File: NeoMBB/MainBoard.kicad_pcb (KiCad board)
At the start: 4 copper layers, 120 x 105 mm, 105 parts, among them IC1 MCP2515-e_ST, IC2 ISO1042BDWVR, IC3 MCP2515-e_ST, IC4 ISO1042BDWVR, J2 TBP01R2-508-06BE, J3 TBP01R1-508-08BE, J4 TBP01R2-508-04BE, J5 TBP01R2-508-04BE, Q1 SIHFR120-GE3, Q2 SIHFR120-GE3, U1 TCMT1100, U11 TCMT1100, U12 BTS462TATMA1, U2 TCMT1100, U3 TCMT1100, U4 TCMT1100, U5 BTS462TATMA1, U6 TCMT1100, U7 TCMT1100, U9 TCMT1100, Y1 8MHz, Y2 8MHz

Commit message: Probed Zero wiring harness
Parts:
- removed C31, C32, C33, C34, C35, C36, C37, C38, C39, C40, C41, C42: UCM1H101MCL1GS, InverterCom:CAPAE660X800N
- removed D1, D2, D3, D4: SM6T15A, Diode_SMD:D_SMB
- removed J5: TBP01R2-508-04BE, InverterCom:SHDR4W100P0X508_1X4_2192X850X1200P
- removed Q2: SIHFR120-GE3, InverterCom:SIHFR120GE3
- removed R12, R16, R19, R24: 1k, Resistor_SMD:R_1210_3225Metric_Pad1.30x2.65mm_HandSolder
- removed R13, R14, R15, R17, R18, R20, R21, R25, R26: 4.7k, Resistor_SMD:R_1210_3225Metric_Pad1.30x2.65mm_HandSolder
- removed R22, R23: 120, Resistor_SMD:R_1210_3225Metric_Pad1.30x2.65mm_HandSolder
- removed U1, U11, U2, U3, U4, U6, U7, U9: TCMT1100, Package_SO:SOP-4_4.4x2.6mm_P1.27mm
- removed U12, U5: BTS462TATMA1, Package_TO_SOT_SMD:TO-252-4
- added C43: 100nF, Capacitor_SMD:C_1210_3225Metric_Pad1.33x2.70mm_HandSolder, F.Cu at (-38.6, 124.5)
- added C44: 22pF, Capacitor_SMD:C_1210_3225Metric_Pad1.33x2.70mm_HandSolder, F.Cu at (-38.6, 128.8)
- added C45: 10uF, Capacitor_SMD:C_1210_3225Metric_Pad1.33x2.70mm_HandSolder, F.Cu at (-38.6, 133.0)
- added C46: 10uF, Capacitor_SMD:C_1210_3225Metric_Pad1.33x2.70mm_HandSolder, F.Cu at (-38.6, 137.3)
- added C47: 10uF, Capacitor_SMD:C_1210_3225Metric_Pad1.33x2.70mm_HandSolder, F.Cu at (-38.6, 141.5)
- added C48: 22pF, Capacitor_SMD:C_1210_3225Metric_Pad1.33x2.70mm_HandSolder, F.Cu at (-32.6, 124.5)
- added C49: 100nF, Capacitor_SMD:C_1210_3225Metric_Pad1.33x2.70mm_HandSolder, F.Cu at (-32.6, 128.8)
- added C50: 100nF, Capacitor_SMD:C_1210_3225Metric_Pad1.33x2.70mm_HandSolder, F.Cu at (-32.6, 133.0)
- added C51: 10uF, Capacitor_SMD:C_1210_3225Metric_Pad1.33x2.70mm_HandSolder, F.Cu at (-32.6, 137.3)
- added C52: 100nF, Capacitor_SMD:C_1210_3225Metric_Pad1.33x2.70mm_HandSolder, F.Cu at (-32.6, 141.5)
- added C53: 22pF, Capacitor_SMD:C_1210_3225Metric_Pad1.33x2.70mm_HandSolder, F.Cu at (-26.6, 124.5)
- added C54: 22pF, Capacitor_SMD:C_1210_3225Metric_Pad1.33x2.70mm_HandSolder, F.Cu at (-26.6, 128.8)
- added C55: 22pF, Capacitor_SMD:C_1210_3225Metric_Pad1.33x2.70mm_HandSolder, F.Cu at (-26.6, 133.0)
- added C56: 100nF, Capacitor_SMD:C_1210_3225Metric_Pad1.33x2.70mm_HandSolder, F.Cu at (-38.6, 89.5)
- added C57: 22pF, Capacitor_SMD:C_1210_3225Metric_Pad1.33x2.70mm_HandSolder, F.Cu at (-38.6, 93.7)
- added C58: 10uF, Capacitor_SMD:C_1210_3225Metric_Pad1.33x2.70mm_HandSolder, F.Cu at (-38.6, 98.0)
- added C59: 10uF, Capacitor_SMD:C_1210_3225Metric_Pad1.33x2.70mm_HandSolder, F.Cu at (-38.6, 102.2)
- added C60: 10uF, Capacitor_SMD:C_1210_3225Metric_Pad1.33x2.70mm_HandSolder, F.Cu at (-38.6, 106.5)
- added C61: 22pF, Capacitor_SMD:C_1210_3225Metric_Pad1.33x2.70mm_HandSolder, F.Cu at (-32.6, 89.5)
- added C62: 100nF, Capacitor_SMD:C_1210_3225Metric_Pad1.33x2.70mm_HandSolder, F.Cu at (-32.6, 93.7)
- added C63: 100nF, Capacitor_SMD:C_1210_3225Metric_Pad1.33x2.70mm_HandSolder, F.Cu at (-32.6, 98.0)
- added C64: 10uF, Capacitor_SMD:C_1210_3225Metric_Pad1.33x2.70mm_HandSolder, F.Cu at (-32.6, 102.2)
- added C65: 100nF, Capacitor_SMD:C_1210_3225Metric_Pad1.33x2.70mm_HandSolder, F.Cu at (-32.6, 106.5)
- added C66: 22pF, Capacitor_SMD:C_1210_3225Metric_Pad1.33x2.70mm_HandSolder, F.Cu at (-26.6, 89.5)
- added C67: 22pF, Capacitor_SMD:C_1210_3225Metric_Pad1.33x2.70mm_HandSolder, F.Cu at (-26.6, 93.7)
- added C68: 22pF, Capacitor_SMD:C_1210_3225Metric_Pad1.33x2.70mm_HandSolder, F.Cu at (-26.6, 98.0)
- added C76: 10nF, Capacitor_SMD:C_1210_3225Metric_Pad1.33x2.70mm_HandSolder, F.Cu at (-55.3, 128.1)
- added C77: 10nF, Capacitor_SMD:C_1210_3225Metric_Pad1.33x2.70mm_HandSolder, F.Cu at (-55.3, 132.4)
- added C78: 10nF, Capacitor_SMD:C_1210_3225Metric_Pad1.33x2.70mm_HandSolder, F.Cu at (-55.3, 136.6)
- added C79: 10nF, Capacitor_SMD:C_1210_3225Metric_Pad1.33x2.70mm_HandSolder, F.Cu at (-55.3, 140.9)
- added FL3: ACT45B-101-2P-TL003, InverterCom:ACT45B1012PTL003, F.Cu at (-14.8, 113.8)
- added FL4: ACT45B-101-2P-TL003, InverterCom:ACT45B1012PTL003, F.Cu at (-14.8, 78.7)
- added IC10: DRDNB21D-7, InverterCom:SOT65P210X110-6N, B.Cu at (91.0, 22.5)
- added IC11: DRDNB21D-7, InverterCom:SOT65P210X110-6N, B.Cu at (113.5, 33.1)
- added IC5: MCP2515-e_ST, InverterCom:SOP65P640X120-20N, F.Cu at (-19.1, 140.2)
- added IC6: ISO1042BDWVR, InverterCom:SOIC127P1150X280-8N, F.Cu at (-16.7, 125.9)
- added IC7: MCP2515-e_ST, InverterCom:SOP65P640X120-20N, F.Cu at (-19.1, 105.2)
- added IC8: ISO1042BDWVR, InverterCom:SOIC127P1150X280-8N, F.Cu at (-16.7, 90.9)
- added IC9: MCP23S17-E_SO, InverterCom:SOIC127P1030X265-28N, F.Cu at (122.2, 58.1)
- added J1: MX23A34NF1, InverterCom:MX23A34NF1, F.Cu at (115.0, -6.00)
- added JP1: Jumper_2_Open, Jumper:SolderJumper-3_P2.0mm_Open_TrianglePad1.0x1.5mm, F.Cu at (22.5, 22.5)
- added JP2: Jumper_2_Open, Jumper:SolderJumper-3_P2.0mm_Open_TrianglePad1.0x1.5mm, F.Cu at (22.5, 26.4)
- added JP3: Jumper_2_Open, Jumper:SolderJumper-3_P2.0mm_Open_TrianglePad1.0x1.5mm, F.Cu at (22.5, 30.2)
- added JP4: Jumper_2_Open, Jumper:SolderJumper-3_P2.0mm_Open_TrianglePad1.0x1.5mm, F.Cu at (22.5, 34.1)
- added K1: AWHSH105D00G, InverterCom:AWHSH105D00G, F.Cu at (108.3, 16.5)
- added K2: AWHSH105D00G, InverterCom:AWHSH105D00G, F.Cu at (74.2, 28.5)
- added K3: AWHSH105D00G, InverterCom:AWHSH105D00G, F.Cu at (52.8, 28.5)
- added K4: AWHSH105D00G, InverterCom:AWHSH105D00G, F.Cu at (119.2, 28.5)
- added PS5: RKE-1205S_H, InverterCom:RKE1205SH, F.Cu at (-38.0, 115.0)
- added PS6: RKE-1205S_H, InverterCom:RKE1205SH, F.Cu at (-38.0, 80.0)
- added R27: 4.7k, Resistor_SMD:R_1210_3225Metric_Pad1.30x2.65mm_HandSolder, F.Cu at (-11.7, 138.2)
- added R28: 120, Resistor_SMD:R_1210_3225Metric_Pad1.30x2.65mm_HandSolder, F.Cu at (-11.7, 142.5)
- added R29: 4.7k, Resistor_SMD:R_1210_3225Metric_Pad1.30x2.65mm_HandSolder, F.Cu at (-11.7, 103.2)
- added R30: 120, Resistor_SMD:R_1210_3225Metric_Pad1.30x2.65mm_HandSolder, F.Cu at (-11.7, 107.4)
- added R38: 10k, Resistor_SMD:R_1210_3225Metric_Pad1.30x2.65mm_HandSolder, F.Cu at (-82.8, 88.7)
- added R40: 1k, Resistor_SMD:R_1210_3225Metric_Pad1.30x2.65mm_HandSolder, F.Cu at (-49.4, 128.1)
- added R41: 1k, Resistor_SMD:R_1210_3225Metric_Pad1.30x2.65mm_HandSolder, F.Cu at (-49.4, 132.3)
- added R42: 1k, Resistor_SMD:R_1210_3225Metric_Pad1.30x2.65mm_HandSolder, F.Cu at (-49.4, 136.5)
- added R43: 1k, Resistor_SMD:R_1210_3225Metric_Pad1.30x2.65mm_HandSolder, F.Cu at (-49.4, 140.7)
- added Y3: 8MHz, Crystal:Crystal_HC49-4H_Vertical, F.Cu at (-19.4, 132.8)
- added Y4: 8MHz, Crystal:Crystal_HC49-4H_Vertical, F.Cu at (-19.4, 97.8)
- added Z10: MMSZ5231B-TP, InverterCom:SOD3716X135N, F.Cu at (-61.4, 141.2)
- added Z11: MMSZ5231B-TP, InverterCom:SOD3716X135N, F.Cu at (-61.4, 121.8)
- added Z2: MMSZ5231B-TP, InverterCom:SOD3716X135N, F.Cu at (-61.4, 128.2)
- added Z5: MMSZ5231B-TP, InverterCom:SOD3716X135N, F.Cu at (-61.4, 108.7)
- added Z6: MMSZ5231B-TP, InverterCom:SOD3716X135N, F.Cu at (-61.4, 113.1)
- added Z7: MMSZ5231B-TP, InverterCom:SOD3716X135N, F.Cu at (-61.4, 117.4)
- added Z8: MMSZ5231B-TP, InverterCom:SOD3716X135N, F.Cu at (-61.4, 132.5)
- added Z9: MMSZ5231B-TP, InverterCom:SOD3716X135N, F.Cu at (-61.4, 136.9)
- A1: footprint Module:RaspberryPi_Pico_Common_Unspecified -> Module:RaspberryPi_Pico_Common_THT
- C1, C10, C11, C12, C15, C16, C17, C19, C2, C20, C21, C22, C23, C24, C25, C3, C4, C5, C6, C7, C8, C9, R2, R3, R4: moved to F.Cu
- C27, C28, C29, C30: value UCM1H101MCL1GS -> 10nF; footprint InverterCom:CAPAE660X800N -> Capacitor_SMD:C_1210_3225Metric_Pad1.33x2.70mm_HandSolder
- J2: value TBP01R2-508-06BE -> MX23A40NF1; footprint InverterCom:TBP01R250806BE -> InverterCom:MX23A40NF1
- J3: value TBP01R1-508-08BE -> TBP02R2W-381-06BE; footprint InverterCom:SHDR8W100P0X508_1X8_4224X1200X890P -> InverterCom:TBP02R2W38106BE
- PS1: value SCW20A-12 -> OKI-78SR-5_1.5-W36E-C; footprint InverterCom:SCW20A12 -> InverterCom:OKI78SR515W36EC
- PS4: value R-78K3.3-1.0 -> EC7BW-110S12; footprint InverterCom:R78K3310 -> InverterCom:EC7BW110S12; moved to B.Cu
- Q1: value SIHFR120-GE3 -> TBD62783AFG,EL; footprint InverterCom:SIHFR120GE3 -> InverterCom:SOIC127P1030X245-18N; moved to B.Cu
- R10: value 4.7k -> 0
- R11, R9: value 1k -> 0
- R6, R8: value 4.7k -> 1k
- moved C24 198.3 mm to (-84.4, 119.5)
- moved C25 197.4 mm to (-84.4, 123.7), turned to 0 degrees
- moved C26 193.9 mm to (-84.4, 128.0), turned to 0 degrees
- moved C23 192.2 mm to (-90.4, 136.5), turned to 0 degrees
- moved C22 186.9 mm to (-90.4, 132.2), turned to 0 degrees
- moved C17 179.7 mm to (-96.4, 132.2)
- moved C16 179.0 mm to (-96.4, 128.0), turned to 0 degrees
- moved R4 177.5 mm to (-69.5, 137.4), turned to 0 degrees
- moved C21 176.7 mm to (-90.4, 128.0), turned to 0 degrees
- moved C15 175.0 mm to (-96.4, 123.7), turned to 0 degrees
- moved R9 174.6 mm to (-82.8, 76.0), turned to 0 degrees
- moved R11 173.6 mm to (-82.8, 84.5), turned to 0 degrees
- moved PS3 171.9 mm to (-95.9, 110.0)
- moved C18 171.3 mm to (-96.4, 136.5), turned to 0 degrees
- moved H2 170.7 mm to (152.5, 7.50)
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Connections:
- A1 pad 10: /CHARGER_OUT_SS1 -> /CAN2_INT
- A1 pad 11: /CHARGER_OUT_SS2 -> /UART_TX
- A1 pad 12: /CHARGER_IN_DCP -> /UART_RX
- A1 pad 13: /GND_A -> /12V_GND
- A1 pad 14: /CAN2_SPI_SCK -> /MCP_SPI_SCK
- A1 pad 15: /CAN2_SPI_TX -> /MCP_SPI_TX
- A1 pad 16: /CAN2_SPI_RX -> /MCP_SPI_RX
- A1 pad 17: /CAN2_INT -> /CAN2_CS
- A1 pad 18: /GND_A -> /12V_GND
- A1 pad 19: /CAN2_CS -> /CAN3_INT
- A1 pad 20: /CONTACTOR_OUT -> /CAN3_CS
- A1 pad 21: /VEHICLE_IN_SS1 -> /CAN4_CS
- A1 pad 22: /VEHICLE_IN_SS2 -> /CAN4_INT
- A1 pad 23: /GND_A -> /12V_GND
- A1 pad 24: /VEHICLE_IN_PP -> /MCP_SPI_CS
- A1 pad 25: /VEHICLE_OUT_DCP -> /MCP_SPI_INTA
- A1 pad 26: unconnected-(A1-GPIO20-Pad26) -> /MCP_SPI_INTB
- A1 pad 27: unconnected-(A1-GPIO21-Pad27) -> /MCP_SPI_RST
- A1 pad 28: /GND_A -> /12V_GND
- A1 pad 29: unconnected-(A1-GPIO22-Pad29) -> /MTR_CTRL_ENABLE_SIGNAL
- A1 pad 3: /GND_A -> /12V_GND
- A1 pad 31: unconnected-(A1-GPIO26_ADC0-Pad31) -> /AMBIENT_TEMP
- A1 pad 33: /GND_A -> /12V_GND
- A1 pad 38: /GND_A -> /12V_GND
- A1 pad 4: /CAN1_SPI_SCK -> /CAN_SPI_SCK
- A1 pad 5: /CAN1_SPI_TX -> /CAN_SPI_TX
- A1 pad 6: /CAN1_SPI_RX -> /CAN_SPI_RX
- A1 pad 8: /GND_A -> /12V_GND
- C1 pad 2: /GND_A -> /12V_GND
- C10 pad 1: /Isolated Canbus Module/CAN_GND -> /CAN0_GND
- C10 pad 2: /Isolated Canbus Module/CAN_5V -> /CAN0_+5V
- C11 pad 1: /Isolated Canbus Module/CAN_GND -> /CAN0_GND
- C11 pad 2: /Isolated Canbus Module/CAN_H_B -> /CAN0_HIGH
- C12 pad 1: /Isolated Canbus Module/CAN_L_B -> /CAN0_LOW
- C12 pad 2: /Isolated Canbus Module/CAN_GND -> /CAN0_GND
- C13 pad 1: /Isolated Canbus Module/CAN_H_B -> /CAN0_HIGH
- C13 pad 2: /Isolated Canbus Module/CAN_L_B -> /CAN0_LOW
- C14 pad 2: /GND_A -> /12V_GND
- C15 pad 2: /GND_A -> /12V_GND
- C16 pad 1: /GND_A -> /12V_GND
- C17 pad 2: /GND_A -> /12V_GND
- C18 pad 2: /GND_A -> /12V_GND
- C19 pad 2: /GND_A -> /12V_GND
- C2 pad 2: /GND_A -> /12V_GND
- C20 pad 2: /GND_A -> /12V_GND
- C21 pad 2: /GND_A -> /12V_GND
- C22 pad 2: /CHAdeMO_FG -> /CAN1_GND
- C23 pad 1: /CHAdeMO_FG -> /CAN1_GND
- C24 pad 1: /CHAdeMO_FG -> /CAN1_GND
- C24 pad 2: /CHAdeMO_CAN_H -> /CAN1_HIGH
- C25 pad 1: /CHAdeMO_CAN_L -> /CAN1_LOW
- C25 pad 2: /CHAdeMO_FG -> /CAN1_GND
- C26 pad 1: /CHAdeMO_CAN_H -> /CAN1_HIGH
- C26 pad 2: /CHAdeMO_CAN_L -> /CAN1_LOW
- C27 pad 1: /+12V_A -> /KICKSTAND_SW_FILTERED
- C27 pad 2: /GND_A -> /12V_GND
- C28 pad 1: /+12V_A -> /HVIL_SIG_FILTERED
- C28 pad 2: /GND_A -> /12V_GND
- C29 pad 1: /+12V_A -> /MTR_STOP_SW_SIGNAL
- C29 pad 2: /GND_A -> /12V_GND
- C3 pad 1: /GND_A -> /12V_GND
- C30 pad 1: /+12V_A -> /START_SW_INPUT_SIGNAL
- C30 pad 2: /GND_A -> /12V_GND
- C4 pad 2: /GND_A -> /12V_GND
- C5 pad 2: /GND_A -> /12V_GND
- C6 pad 2: /GND_A -> /12V_GND
- C7 pad 2: /GND_A -> /12V_GND
- C8 pad 2: /GND_A -> /12V_GND
- C9 pad 1: /Isolated Canbus Module/CAN_5V -> /CAN0_+5V
- C9 pad 2: /Isolated Canbus Module/CAN_GND -> /CAN0_GND
- FL1 pad 3: /Isolated Canbus Module/CAN_L_B -> /CAN0_LOW
- FL1 pad 4: /Isolated Canbus Module/CAN_H_B -> /CAN0_HIGH
- FL2 pad 3: /CHAdeMO_CAN_L -> /CAN1_LOW
- FL2 pad 4: /CHAdeMO_CAN_H -> /CAN1_HIGH
- IC1 pad 10: /GND_A -> /12V_GND
- IC1 pad 14: /CAN1_SPI_SCK -> /CAN_SPI_SCK
- IC1 pad 16: /CAN1_SPI_TX -> /CAN_SPI_TX
- IC1 pad 17: /CAN1_SPI_RX -> /CAN_SPI_RX
- IC2 pad 4: /GND_A -> /12V_GND
- IC2 pad 5: /Isolated Canbus Module/CAN_GND -> /CAN0_GND
- IC2 pad 8: /Isolated Canbus Module/CAN_5V -> /CAN0_+5V
- IC3 pad 10: /GND_A -> /12V_GND
- IC3 pad 14: /CAN2_SPI_SCK -> /CAN_SPI_SCK
- IC3 pad 16: /CAN2_SPI_TX -> /CAN_SPI_TX
- IC3 pad 17: /CAN2_SPI_RX -> /CAN_SPI_RX
- IC4 pad 4: /GND_A -> /12V_GND
- IC4 pad 5: /CHAdeMO_FG -> /CAN1_GND
- J2 pad 1: /Isolated Canbus Module/CAN_5V -> /MOTOR_CONTR_GND
- J2 pad 2: /Isolated Canbus Module/CAN_GND -> /MOTOR_CONTR_+24V_IN
- J2 pad 3: /Isolated Canbus Module/CAN_H_B -> /CAN0_GND
- J2 pad 4: /Isolated Canbus Module/CAN_JUMPER_B -> /CAN0_+5V
- J2 pad 5: /Isolated Canbus Module/CAN_L_B -> /CAN1_GND
- J2 pad 6: /Isolated Canbus Module/CAN_H_B -> /CAN2_HIGH
- J3 pad 1: /CHAdeMO_FG -> unconnected-(J3-Pad1)
- J3 pad 2: /CHAdeMO_SS1 -> unconnected-(J3-Pad2)
- J3 pad 3: /CHAdeMO_SS2 -> /CAN2_GND
- J3 pad 4: /CHAdeMO_NC -> /CAN2_+5V
- J3 pad 5: /CHAdeMO_DCP -> /CAN2_HIGH
- J3 pad 6: /CHAdeMO_PP -> /CAN2_LOW
- J4 pad 1: /GND_A -> /12V_GND
- J4 pad 3: /GND_A -> /12V_GND
- PS1 pad 1: unconnected-(PS1-REMOTE_ON/OFF-Pad1) -> /+12V_A
- PS1 pad 2: /GND_A -> /12V_GND
- PS1 pad 3: /GND_A -> /+5V_A
- PS2 pad 2: /GND_A -> /12V_GND
- PS2 pad 5: /Isolated Canbus Module/CAN_GND -> /CAN0_GND
- PS2 pad 7: /Isolated Canbus Module/CAN_5V -> /CAN0_+5V
- PS3 pad 2: /GND_A -> /12V_GND
- PS3 pad 5: /CHAdeMO_FG -> /CAN1_GND
- PS4 pad 1: /+12V_A -> /MBB_LOW_PWR
- PS4 pad 2: /GND_A -> /POWER_PACK_GND
- PS4 pad 3: /+3.3V_A -> /+12V_A
- Q1 pad 1: Net-(Q1-G) -> /SIG_ABS_LIGHT
- Q1 pad 2: /CHAdeMO_FG -> /SIG_CHARGING_RED
- Q1 pad 3: /CHAdeMO_SS2 -> /SIG_CHARGING
- R10 pad 1: /+3.3V_A -> /POWER_PACK_GND
- R10 pad 2: /CHARGER_IN_DCP -> /HighSideOutputs/RELAY_3_COM
- R11 pad 1: /+12V_CHAdeMO -> /KEY_ON_12V
- R11 pad 2: Net-(R11-Pad2) -> /+12V_A
- R2 pad 2: /Isolated Canbus Module/CAN_L_B -> /CAN0_LOW
- R4 pad 1: /CHAdeMO_CAN_H -> /Isolated Canbus Module1/CAN_JUMPER_B
- R4 pad 2: /CHAdeMO_CAN_L -> /CAN1_LOW
- R5 pad 1: /CHAdeMO_SS1 -> /KICKSTAND_SW_FILTERED
- R5 pad 2: Net-(R5-Pad2) -> /KICKSTAND_SW_SIG
- R6 pad 1: /+3.3V_A -> /HVIL_SIG_FILTERED
- R6 pad 2: /VEHICLE_IN_SS1 -> /HVIL_RETURN
- R7 pad 1: /CHAdeMO_SS1 -> /MTR_STOP_SW_SIGNAL
- R7 pad 2: Net-(R7-Pad2) -> /MTR_STOP_SW_IN
- R8 pad 1: /+3.3V_A -> /START_SW_INPUT_SIGNAL
- R8 pad 2: /VEHICLE_IN_SS2 -> /START_SW_INPUT
- R9 pad 1: /+12V_CHAdeMO -> /MBB_LOW_PWR
- R9 pad 2: Net-(R9-Pad2) -> /HighSideOutputs/RELAY_3_COM
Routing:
- net /+12V_A: track 99.2 -> 0.00 mm, vias 10 -> 0
- net /CHARGER_OUT_SS1: track 85.4 -> 0.00 mm
- net /CHARGER_OUT_SS2: track 78.4 -> 0.00 mm, vias 1 -> 0
- net /CAN1_CS: track 77.7 -> 0.00 mm, vias 3 -> 0
- net /CAN1_INT: track 72.9 -> 0.00 mm
- net /CAN1_SPI_RX: track 71.8 -> 0.00 mm, vias 1 -> 0
- net /CHARGER_IN_DCP: track 70.1 -> 0.00 mm, vias 3 -> 0
- net /CAN1_SPI_TX: track 65.6 -> 0.00 mm, vias 2 -> 0
- net /CAN1_SPI_SCK: track 64.2 -> 0.00 mm
- net /VEHICLE_IN_PP: track 58.0 -> 0.00 mm, vias 6 -> 0
- net /CHAdeMO_SS1: track 57.8 -> 0.00 mm, vias 4 -> 0
- net /+3.3V_A: track 55.6 -> 0.00 mm, vias 13 -> 0
- net /CHAdeMO_SS2: track 51.4 -> 0.00 mm, vias 5 -> 0
- net /VEHICLE_IN_SS2: track 50.6 -> 0.00 mm, vias 6 -> 0
- net /Isolated Canbus Module/CAN_H_B: track 46.5 -> 0.00 mm, vias 1 -> 0
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- removed copper zone on In2.Cu, net /+12V_A
- removed copper zone on In2.Cu, net /+12V_CHAdeMO
- removed copper zone on In2.Cu, net /+3.3V_A
- removed copper zone on B.Cu, net /CHAdeMO_FG
- removed copper zone on F.Cu, net /CHAdeMO_FG
- removed copper zone on In1.Cu, net /CHAdeMO_FG
- removed copper zone on B.Cu, net /GND_A
- removed copper zone on F.Cu, net /GND_A
- removed copper zone on In1.Cu, net /GND_A
- removed copper zone on B.Cu, net /Isolated Canbus Module/CAN_GND
- removed copper zone on F.Cu, net /Isolated Canbus Module/CAN_GND
- removed copper zone on In1.Cu, net /Isolated Canbus Module/CAN_GND
- removed copper zone on In2.Cu, net /Isolated Canbus Module/CAN_GND
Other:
- board size 120 x 105 mm -> 160 x 80 mm
- copper layers 4 -> 6
- board text removed: "->"
- board text removed: "CHAdeMO INTERFACE BOARD CAN FUNCTION AS STATION OR VEHICLE"
- board text removed: "CHAdeMO PP RESISTOR (CHARGER SIDE ONLY)"
- board text removed: "| +5V | GND | JP1 | JP2 | CANL | CANH | CAN 1 INTERFACE"
- board text removed: "| A | B | A | B | 12V <1.5A CONTACTOR COIL"
- board text removed: "| FG | SS1 | SS2 | NC | DCP | PP | CANH| CANL| CHAdeMO SIGNAL PINS"
- board text removed: "| GND | +12V | GND | +12V | 12V INPUT"

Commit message: MBB Reverse engineering bs
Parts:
- removed C27, C28, C29, C30, C76, C77, C78, C79: 10nF, Capacitor_SMD:C_1210_3225Metric_Pad1.33x2.70mm_HandSolder
- removed C58, C59, C60, C64: 10uF, Capacitor_SMD:C_1210_3225Metric_Pad1.33x2.70mm_HandSolder
- removed C61, C66, C67, C68: 22pF, Capacitor_SMD:C_1210_3225Metric_Pad1.33x2.70mm_HandSolder
- removed C62, C63, C65: 100nF, Capacitor_SMD:C_1210_3225Metric_Pad1.33x2.70mm_HandSolder
- removed J3: TBP02R2W-381-06BE, InverterCom:TBP02R2W38106BE
- removed K3, K4: AWHSH105D00G, InverterCom:AWHSH105D00G
- removed R41, R42, R43: 1k, Resistor_SMD:R_1210_3225Metric_Pad1.30x2.65mm_HandSolder
- removed Z10, Z11, Z2, Z5, Z6, Z7, Z8, Z9: MMSZ5231B-TP, InverterCom:SOD3716X135N
- added C31: 100nF, Capacitor_SMD:C_1210_3225Metric_Pad1.33x2.70mm_HandSolder, B.Cu at (17.0, 79.6)
- added C32: 22pF, Capacitor_SMD:C_1210_3225Metric_Pad1.33x2.70mm_HandSolder, B.Cu at (17.0, 63.6)
- added C33: 10uF, Capacitor_SMD:C_1210_3225Metric_Pad1.33x2.70mm_HandSolder, B.Cu at (21.0, 79.4)
- added C34: 10uF, Capacitor_SMD:C_1210_3225Metric_Pad1.33x2.70mm_HandSolder, B.Cu at (33.6, 68.0)
- added C35: 10uF, Capacitor_SMD:C_1210_3225Metric_Pad1.33x2.70mm_HandSolder, B.Cu at (33.0, 75.0)
- added C36: 22pF, Capacitor_SMD:C_1210_3225Metric_Pad1.33x2.70mm_HandSolder, B.Cu at (23.0, 63.4)
- added C37: 100nF, Capacitor_SMD:C_1210_3225Metric_Pad1.33x2.70mm_HandSolder, B.Cu at (28.0, 68.0)
- added C38: 100nF, Capacitor_SMD:C_1210_3225Metric_Pad1.33x2.70mm_HandSolder, B.Cu at (29.0, 75.0)
- added C39: 10uF, Capacitor_SMD:C_1210_3225Metric_Pad1.33x2.70mm_HandSolder, B.Cu at (45.0, 75.0)
- added C40: 100nF, Capacitor_SMD:C_1210_3225Metric_Pad1.33x2.70mm_HandSolder, B.Cu at (40.0, 74.6)
- added C41: 22pF, Capacitor_SMD:C_1210_3225Metric_Pad1.33x2.70mm_HandSolder, F.Cu at (53.0, 75.0)
- added C42: 22pF, Capacitor_SMD:C_1210_3225Metric_Pad1.33x2.70mm_HandSolder, B.Cu at (50.6, 77.0)
- added IC12: DRDNB21D-7, InverterCom:SOT65P210X110-6N, B.Cu at (76.0, 41.6)
- added IC13: DRDNB21D-7, InverterCom:SOT65P210X110-6N, B.Cu at (108.0, 23.0)
- added IC14: DRDNB21D-7, InverterCom:SOT65P210X110-6N, B.Cu at (109.0, 41.0)
- added IC15: MCP23S17-E_SO, InverterCom:SOIC127P1030X265-28N, F.Cu at (86.0, 62.0)
- added K5: AWHSH105D00G, InverterCom:AWHSH105D00G, F.Cu at (116.2, 47.0)
- added K6: AWHSH105D00G, InverterCom:AWHSH105D00G, F.Cu at (95.2, 29.0)
- added K7: AWHSH105D00G, InverterCom:AWHSH105D00G, F.Cu at (116.2, 29.0)
- added K8: AWHSH105D00G, InverterCom:AWHSH105D00G, F.Cu at (95.2, 47.0)
- added PS7: RD7-12S033R, InverterCom:RD712S033R, F.Cu at (156.6, 73.4)
- added PS8: RKE-1205S_H, InverterCom:RKE1205SH, F.Cu at (16.2, 92.1)
- added PS9: RKE-1205S_H, InverterCom:RKE1205SH, F.Cu at (38.0, 92.0)
- added R12: 4.7k, Resistor_SMD:R_1210_3225Metric_Pad1.30x2.65mm_HandSolder, F.Cu at (14.4, 79.0)
- added R13: 120, Resistor_SMD:R_1210_3225Metric_Pad1.30x2.65mm_HandSolder, B.Cu at (51.0, 67.0)
- added R14: 4.7k, Resistor_SMD:R_1210_3225Metric_Pad1.30x2.65mm_HandSolder, F.Cu at (41.0, 54.0)
- added R15: 120, Resistor_SMD:R_1210_3225Metric_Pad1.30x2.65mm_HandSolder, B.Cu at (41.0, 17.4)
- added R16: 0, Resistor_SMD:R_1210_3225Metric_Pad1.30x2.65mm_HandSolder, F.Cu at (-111.3, 134.2)
- added R17: 1k, Resistor_SMD:R_1210_3225Metric_Pad1.30x2.65mm_HandSolder, F.Cu at (-139.0, 140.8)
- added R18: 4.7k, Resistor_SMD:R_1210_3225Metric_Pad1.30x2.65mm_HandSolder, F.Cu at (-139.0, 145.0)
- added R19: 1k, Resistor_SMD:R_1210_3225Metric_Pad1.30x2.65mm_HandSolder, F.Cu at (-87.1, 120.3)
- added R20: 1k, Resistor_SMD:R_1210_3225Metric_Pad1.30x2.65mm_HandSolder, F.Cu at (-87.1, 124.5)
- added R21: 1k, Resistor_SMD:R_1210_3225Metric_Pad1.30x2.65mm_HandSolder, F.Cu at (-87.1, 128.7)
- added R22: 1k, Resistor_SMD:R_1210_3225Metric_Pad1.30x2.65mm_HandSolder, F.Cu at (-87.1, 132.9)
- added R23: 1k, Resistor_SMD:R_1210_3225Metric_Pad1.30x2.65mm_HandSolder, F.Cu at (-87.1, 137.1)
- added R24: 1k, Resistor_SMD:R_1210_3225Metric_Pad1.30x2.65mm_HandSolder, F.Cu at (-87.1, 141.4)
- added R25: 0, Resistor_SMD:R_1210_3225Metric_Pad1.30x2.65mm_HandSolder, F.Cu at (-14.6, -5.00)
- added R26: 0, Resistor_SMD:R_1210_3225Metric_Pad1.30x2.65mm_HandSolder, F.Cu at (-66.4, 2.69)
- added R31: 120, Resistor_SMD:R_1210_3225Metric_Pad1.30x2.65mm_HandSolder, F.Cu at (-52.5, -1.51)
- added R32: 120, Resistor_SMD:R_1210_3225Metric_Pad1.30x2.65mm_HandSolder, F.Cu at (-52.5, 2.69)
- added R33: 120, Resistor_SMD:R_1210_3225Metric_Pad1.30x2.65mm_HandSolder, F.Cu at (-52.5, 6.91)
- added R34: 1k, Resistor_SMD:R_1210_3225Metric_Pad1.30x2.65mm_HandSolder, F.Cu at (-52.5, 11.1)
- added R35: 1k, Resistor_SMD:R_1210_3225Metric_Pad1.30x2.65mm_HandSolder, F.Cu at (-52.5, 15.3)
- added R36: 1k, Resistor_SMD:R_1210_3225Metric_Pad1.30x2.65mm_HandSolder, F.Cu at (-52.5, 19.5)
- added R37: 1k, Resistor_SMD:R_1210_3225Metric_Pad1.30x2.65mm_HandSolder, F.Cu at (-46.5, -1.51)
- added R39: 1k, Resistor_SMD:R_1210_3225Metric_Pad1.30x2.65mm_HandSolder, F.Cu at (-46.5, 2.69)
- added R44: 1k, Resistor_SMD:R_1210_3225Metric_Pad1.30x2.65mm_HandSolder, F.Cu at (-46.5, 6.91)
- added R45: 4.7k, Resistor_SMD:R_1210_3225Metric_Pad1.30x2.65mm_HandSolder, F.Cu at (-46.5, 11.1)
- added R46: 4.7k, Resistor_SMD:R_1210_3225Metric_Pad1.30x2.65mm_HandSolder, F.Cu at (-46.5, 15.3)
- added R47: 10k, Resistor_SMD:R_1210_3225Metric_Pad1.30x2.65mm_HandSolder, F.Cu at (-46.5, 19.5)
- added R48: 1k, Resistor_SMD:R_1210_3225Metric_Pad1.30x2.65mm_HandSolder, F.Cu at (-40.6, -1.51)
- added R49: 1k, Resistor_SMD:R_1210_3225Metric_Pad1.30x2.65mm_HandSolder, F.Cu at (-40.6, 2.69)
- added R50: 1k, Resistor_SMD:R_1210_3225Metric_Pad1.30x2.65mm_HandSolder, F.Cu at (-40.6, 6.91)
- added R51: 1k, Resistor_SMD:R_1210_3225Metric_Pad1.30x2.65mm_HandSolder, F.Cu at (-40.6, 11.1)
- added R52: 4.7k, Resistor_SMD:R_1210_3225Metric_Pad1.30x2.65mm_HandSolder, F.Cu at (-40.6, 15.3)
- added R53: 0, Resistor_SMD:R_1210_3225Metric_Pad1.30x2.65mm_HandSolder, F.Cu at (-103.4, 130.0)
- added U1: TCMT1100, Package_SO:SOP-4_4.4x2.6mm_P1.27mm, F.Cu at (-146.7, 140.8)
- added U2: TCMT1100, Package_SO:SOP-4_4.4x2.6mm_P1.27mm, F.Cu at (-52.0, 37.0)
- added U3: TCMT1100, Package_SO:SOP-4_4.4x2.6mm_P1.27mm, F.Cu at (-39.8, 87.4)
- added U4: TCMT1100, Package_SO:SOP-4_4.4x2.6mm_P1.27mm, F.Cu at (-39.8, 91.5)
- added U5: TCMT1100, Package_SO:SOP-4_4.4x2.6mm_P1.27mm, F.Cu at (-39.8, 95.7)
- added Z1: MMSZ5231B-TP, InverterCom:SOD3716X135N, F.Cu at (-81.0, 137.0)
- added Z12: MMSZ5231B-TP, InverterCom:SOD3716X135N, F.Cu at (-34.5, 13.8)
- added Z13: MMSZ5231B-TP, InverterCom:SOD3716X135N, F.Cu at (-34.5, 18.1)
- added Z14: MMSZ5231B-TP, InverterCom:SOD3716X135N, F.Cu at (-34.5, 22.5)
- added Z15: MMSZ5231B-TP, InverterCom:SOD3716X135N, F.Cu at (-34.5, 26.8)
- added Z16: MMSZ5231B-TP, InverterCom:SOD3716X135N, F.Cu at (-34.5, 31.2)
- added Z3: MMSZ5231B-TP, InverterCom:SOD3716X135N, F.Cu at (-81.0, 141.3)
- added Z4: MMSZ5231B-TP, InverterCom:SOD3716X135N, F.Cu at (-34.5, 9.39)
- C1, C10, C11, C12, C14, C15, C16, C17, C18, C19, C2, C20, C21, C22, C23, C24, C25, C3, C4, C46, C47, C5, C50, C54, C55, C6, C7, C8, C9, R2, R4: moved to B.Cu
- C43, C49: value 100nF -> 22pF; moved to B.Cu
- C44, C53: value 22pF -> 100nF; moved to B.Cu
- C45: value 10uF -> 22pF; moved to B.Cu
- C48: value 22pF -> 10uF; moved to B.Cu
- C51: value 10uF -> 100nF; moved to B.Cu
- C52: value 100nF -> 10uF; moved to B.Cu
- C56: value 100nF -> 22pF
- C57: value 22pF -> 100nF
- IC10, PS4, Q1: moved to F.Cu
- R10, R9: value 0 -> 1k
- R27, R29: value 4.7k -> 1k
- R28: value 120 -> 1k
- R40, R6, R8: value 1k -> 4.7k
- R5: value 1k -> 120
- R7: value 1k -> 10k
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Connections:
- net /ABS_ENABLE renamed /Control/O_SYSTEM_ON_A
- net /CAN_SPI_RX renamed /Control/CAN_SPI_RX
- net /CAN_SPI_SCK renamed /Control/CAN_SPI_SCK
- net /CAN_SPI_TX renamed /Control/CAN_SPI_TX
- net /HighSideOutputs/COIL_1 renamed Net-(IC10-B1)
- net /MCP_SPI_CS renamed /Control/MCP_SPI_CS
- net /MCP_SPI_INTA renamed /Control/MCP_SPI_INTA
- net /MCP_SPI_INTB renamed /Control/MCP_SPI_INTB
- net /MCP_SPI_RST renamed /Control/MCP_SPI_RST
- net /MCP_SPI_RX renamed /Control/MCP_SPI_RX
- net /MCP_SPI_SCK renamed /Control/MCP_SPI_SCK
- net /MCP_SPI_TX renamed /Control/MCP_SPI_TX
- net /MOTOR_CONTR_+24V_IN renamed /NC_INPUT_SEVCON_+24V_C
- A1 pad 1: unconnected-(A1-GPIO0-Pad1) -> /Control/MCP_SPI_RST2
- A1 pad 10: /CAN2_INT -> /Control/CAN2_INT
- A1 pad 13: /12V_GND -> /DIAG_GND
- A1 pad 17: /CAN2_CS -> /Control/CAN2_CS
- A1 pad 18: /12V_GND -> /DIAG_GND
- A1 pad 19: /CAN3_INT -> /Control/CAN3_INT
- A1 pad 2: unconnected-(A1-GPIO1-Pad2) -> /Control/MCP_SPI_CS2
- A1 pad 20: /CAN3_CS -> /Control/CAN3_CS
- A1 pad 21: /CAN4_CS -> /Control/CAN4_CS
- A1 pad 22: /CAN4_INT -> /Control/CAN4_INT
- A1 pad 23: /12V_GND -> /DIAG_GND
- A1 pad 28: /12V_GND -> /DIAG_GND
- A1 pad 29: /MTR_CTRL_ENABLE_SIGNAL -> /Control/MTR_CTRL_ENABLE_SIGNAL
- A1 pad 3: /12V_GND -> /DIAG_GND
- A1 pad 31: /AMBIENT_TEMP -> /INPUT_AMBIENT_TEMP_A
- A1 pad 32: unconnected-(A1-GPIO27_ADC1-Pad32) -> /Control/MCP_SPI_INT2A
- A1 pad 33: /12V_GND -> /DIAG_GND
- A1 pad 34: unconnected-(A1-GPIO28_ADC2-Pad34) -> /Control/MCP_SPI_INT2B
- A1 pad 38: /12V_GND -> /DIAG_GND
- A1 pad 7: /CAN1_INT -> /Control/CAN1_INT
- A1 pad 8: /12V_GND -> /DIAG_GND
- A1 pad 9: /CAN1_CS -> /Control/CAN1_CS
- C1 pad 2: /12V_GND -> /DIAG_GND
- C10 pad 1: /CAN0_GND -> /SEVCON_GND_C
- C10 pad 2: /CAN0_+5V -> /Control/Isolated Canbus Module3/CAN_5V
- C11 pad 1: /CAN0_GND -> /SEVCON_GND_C
- C11 pad 2: /CAN0_HIGH -> /IO_MOTOR_CONTR_CAN_HIGH_C
- C12 pad 1: /CAN0_LOW -> /IO_MOTOR_CONTR_CAN_LOW_C
- C12 pad 2: /CAN0_GND -> /SEVCON_GND_C
- C13 pad 1: /CAN0_HIGH -> /IO_MOTOR_CONTR_CAN_HIGH_C
- C13 pad 2: /CAN0_LOW -> /IO_MOTOR_CONTR_CAN_LOW_C
- C14 pad 2: /12V_GND -> /DIAG_GND
- C15 pad 2: /12V_GND -> /DIAG_GND
- C16 pad 1: /12V_GND -> /DIAG_GND
- C17 pad 2: /12V_GND -> /DIAG_GND
- C18 pad 2: /12V_GND -> /DIAG_GND
- C19 pad 2: /12V_GND -> /DIAG_GND
- C2 pad 2: /12V_GND -> /DIAG_GND
- C20 pad 2: /12V_GND -> /DIAG_GND
- C21 pad 2: /12V_GND -> /DIAG_GND
- C22 pad 1: /Isolated Canbus Module1/CAN_5V -> /CAN2_+5V_G
- C22 pad 2: /CAN1_GND -> /CAN2_GND_G
- C23 pad 1: /CAN1_GND -> /CAN2_GND_G
- C23 pad 2: /Isolated Canbus Module1/CAN_5V -> /CAN2_+5V_G
- C24 pad 1: /CAN1_GND -> /CAN2_GND_G
- C24 pad 2: /CAN1_HIGH -> /IO_CAN2_HIGH_G
- C25 pad 1: /CAN1_LOW -> /IO_CAN2_LOW_G
- C25 pad 2: /CAN1_GND -> /CAN2_GND_G
- C26 pad 1: /CAN1_HIGH -> /IO_CAN2_HIGH_G
- C26 pad 2: /CAN1_LOW -> /IO_CAN2_LOW_G
- C3 pad 1: /12V_GND -> /DIAG_GND
- C4 pad 2: /12V_GND -> /DIAG_GND
- C43 pad 1: /+3.3V_A -> /IO_CAN1_HIGH_F
- C43 pad 2: /12V_GND -> /IO_CAN1_LOW_F
- C44 pad 1: Net-(IC5-OSC2) -> /+3.3V_A
- C44 pad 2: /12V_GND -> /DIAG_GND
- C45 pad 1: /12V_GND -> Net-(IC7-OSC2)
- C45 pad 2: /+3.3V_A -> /DIAG_GND
- C46 pad 1: /+12V_A -> /DIAG_GND
- C46 pad 2: /12V_GND -> /+3.3V_A
- C47 pad 1: /+3.3V_A -> /+12V_A
- C47 pad 2: /12V_GND -> /DIAG_GND
- C48 pad 1: Net-(IC5-OSC1) -> /+3.3V_A
- C48 pad 2: /12V_GND -> /DIAG_GND
- C49 pad 1: /+12V_A -> Net-(IC7-OSC1)
- C49 pad 2: /12V_GND -> /DIAG_GND
- C5 pad 2: /12V_GND -> /DIAG_GND
- C50 pad 1: /+3.3V_A -> /+12V_A
- C50 pad 2: /12V_GND -> /DIAG_GND
- C51 pad 1: /CAN2_+5V -> /+3.3V_A
- C51 pad 2: /CAN2_GND -> /DIAG_GND
- C52 pad 1: /CAN2_GND -> /OUTPUT_CAN0_+5V_E
- C52 pad 2: /CAN2_+5V -> /CAN0_GND_E
- C53 pad 1: /CAN2_GND -> /CAN0_GND_E
- C53 pad 2: /CAN2_HIGH -> /OUTPUT_CAN0_+5V_E
- C54 pad 1: /CAN2_LOW -> /CAN0_GND_E
- C54 pad 2: /CAN2_GND -> /IO_CAN0_HIGH_E
- C55 pad 1: /CAN2_HIGH -> /IO_CAN0_LOW_E
- C55 pad 2: /CAN2_LOW -> /CAN0_GND_E
- C56 pad 1: /+3.3V_A -> /IO_CAN0_HIGH_E
- C56 pad 2: /12V_GND -> /IO_CAN0_LOW_E
- C57 pad 1: Net-(IC7-OSC2) -> /+5V_A
- C57 pad 2: /12V_GND -> /DIAG_GND
- C6 pad 2: /12V_GND -> /DIAG_GND
- C7 pad 2: /12V_GND -> /DIAG_GND
- C8 pad 2: /12V_GND -> /DIAG_GND
- C9 pad 1: /CAN0_+5V -> /Control/Isolated Canbus Module3/CAN_5V
- C9 pad 2: /CAN0_GND -> /SEVCON_GND_C
- FL1 pad 3: /CAN0_LOW -> /IO_MOTOR_CONTR_CAN_LOW_C
- FL1 pad 4: /CAN0_HIGH -> /IO_MOTOR_CONTR_CAN_HIGH_C
- FL2 pad 3: /CAN1_LOW -> /IO_CAN2_LOW_G
- FL2 pad 4: /CAN1_HIGH -> /IO_CAN2_HIGH_G
- FL3 pad 3: /CAN2_LOW -> /IO_CAN1_LOW_F
- FL3 pad 4: /CAN2_HIGH -> /IO_CAN1_HIGH_F
- FL4 pad 3: /MOTOR_CONTR_CAN_LOW -> /IO_CAN0_LOW_E
- FL4 pad 4: /MOTOR_CONTR_CAN_HIGH -> /IO_CAN0_HIGH_E
- IC1 pad 10: /12V_GND -> /DIAG_GND
- IC1 pad 13: /CAN1_INT -> /Control/CAN4_INT
- IC1 pad 18: /CAN1_CS -> /Control/CAN4_CS
- IC10 pad 2: /12V_GND -> /DIAG_GND
- IC10 pad 3: /MTR_CTRL_ENABLE_SIGNAL -> /DIAG_GND
- IC10 pad 4: /HighSideOutputs/COIL_2 -> unconnected-(IC10-B2-Pad4)
- IC11 pad 1: /MTR_CTRL_NEUTRAL_SIGNAL -> /Charger Interface/OUTPUT_OBC_ENABLE_+3.3V_A
- IC11 pad 2: /12V_GND -> /DIAG_GND
- IC11 pad 3: /DCDC_ENABLE_SIGNAL -> /DIAG_GND
- IC11 pad 4: /HighSideOutputs/COIL_4 -> unconnected-(IC11-B2-Pad4)
- IC11 pad 5: /+5V_A -> /Charger Interface/+5V_A
- IC11 pad 6: /HighSideOutputs/COIL_3 -> Net-(IC11-B1)
- IC2 pad 4: /12V_GND -> /DIAG_GND
- IC2 pad 5: /CAN0_GND -> /SEVCON_GND_C
- IC2 pad 8: /CAN0_+5V -> /Control/Isolated Canbus Module3/CAN_5V
- IC3 pad 10: /12V_GND -> /DIAG_GND
- IC3 pad 13: /CAN2_INT -> /Control/CAN3_INT
- IC3 pad 18: /CAN2_CS -> /Control/CAN3_CS
- IC4 pad 4: /12V_GND -> /DIAG_GND
- IC4 pad 5: /CAN1_GND -> /CAN2_GND_G
- IC4 pad 8: /Isolated Canbus Module1/CAN_5V -> /CAN2_+5V_G
- IC5 pad 10: /12V_GND -> /DIAG_GND
- IC5 pad 13: /CAN3_INT -> /Control/CAN2_INT
- IC5 pad 18: /CAN3_CS -> /Control/CAN2_CS
- IC6 pad 4: /12V_GND -> /DIAG_GND
- IC6 pad 5: /CAN2_GND -> /CAN1_GND_F
- IC6 pad 8: /CAN2_+5V -> /Control/Isolated Canbus Module1/CAN_5V
- IC7 pad 10: /12V_GND -> /DIAG_GND
- IC7 pad 13: /CAN4_INT -> /Control/CAN1_INT
- IC7 pad 18: /CAN4_CS -> /Control/CAN1_CS
- IC8 pad 4: /12V_GND -> /DIAG_GND
- IC8 pad 5: /MOTOR_CONTR_GND -> /CAN0_GND_E
- IC8 pad 8: /Isolated Canbus Module3/CAN_5V -> /OUTPUT_CAN0_+5V_E
- IC9 pad 1: /SIG_ABS_LIGHT -> /Control/I_MOTOR_STOP_SW_A
- IC9 pad 15: /12V_GND -> /DIAG_GND
- IC9 pad 16: /12V_GND -> /DIAG_GND
- IC9 pad 17: /12V_GND -> /DIAG_GND
- IC9 pad 2: /SIG_CHARGING_RED -> /Control/I_KICKSTAND_SWITCH_A
- IC9 pad 21: /KICKSTAND_SW_FILTERED -> /Control/O_DASH_CHK_ENG_A
- IC9 pad 22: /HVIL_SIG_FILTERED -> /Control/O_DASH_CHG_RED_A
- IC9 pad 23: /MTR_STOP_SW_SIGNAL -> /Control/O_DASH_CHG_A
- IC9 pad 24: /START_SW_INPUT_SIGNAL -> /Control/O_DASH_ARMED_A
- IC9 pad 25: /BRAKE_SW_INPUT_SIGNAL -> /Control/O_DASH_ABS_A
- IC9 pad 27: /MTR_CTRL_NEUTRAL_SIGNAL -> /Control/I_SYSTEM_ON_REF_A
- IC9 pad 28: /DCDC_ENABLE_SIGNAL -> /Control/I_MOTOR_START_SW_A
- IC9 pad 3: /SIG_CHARGING -> /Control/I_KEY_ON_A
- IC9 pad 4: /SIG_SYS_ARMED -> /Control/I_BRAKE_SWITCH_A
- IC9 pad 5: /SIG_SYS_WARN -> /Control/I_THROTTLE_ENABLE_A
- IC9 pad 6: /SIG_OVERTEMP -> /Control/O_SEVCON_NEUTRAL_A
- IC9 pad 7: /SIG_CHECK_ENG -> /Control/O_DCDC_ENABLE_A
- IC9 pad 8: /SYSTEM_ON_SIGNAL -> /Control/O_SEVCON_ENABLE_A
- J1 pad 1: /MTR_CTRL_ENABLE -> /OUTPUT_SEVCON_ENABLE_+VBATT_C
- J1 pad 11: /KICKSTAND_SW_SIG -> /INPUT_KICKSTAND_SWITCH_+5V_D
- J1 pad 12: /12V_GND -> /KICKSTAND_SWITCH_GND_D
- J1 pad 13: /INST_CLUSTER_CHK_ENG -> /OUTPUT_INST_CLUST_CHK_ENG_+5V_B
- J1 pad 14: /FUEL_GATE_5V_REF -> /OUTPUT_INST_CLUST_SUPPLY_+5V_B
- J1 pad 15: /KEY_ON_12V -> /KEY_ON_+12V_A
- J1 pad 16: /INST_CLUSTER_OVERTEMP -> /OUTPUT_INST_CLUST_OVERTEMP_+5V_B
- J1 pad 17: /INST_CLUSTER_SYS_WARN -> /OUTPUT_INST_CLUST_SYS_WARN_+5V_B
- J1 pad 18: /MBB_LOW_PWR -> /TRBATT_B+_C
- J1 pad 19: /MTR_CTRL_NEUTRAL -> /OUTPUT_SEVCON_NEUTRAL_+VBATT_C
- J1 pad 20: /DC/DC_CONV_ENABLE -> /OUTPUT_DCDC_ENABLE_+VBATT_C
- J1 pad 22: /BATTERY_THROTTLE_ENABLE -> /INPUT_BATTERY_THROTTLE_ENABLE_+5V_A
- J1 pad 23: /+5V_A -> /OUTPUT_MTR_STOP_SWITCH_+5V_D
- J1 pad 24: /MTR_STOP_SW_IN -> /INPUT_MTR_STOP_SWITCH_SIGNAL_+5V_D
- J1 pad 27: /+5V_A -> /OUTPUT_KICKSTAND_SWITCH_+5V_D
- J1 pad 28: /BRAKE_SW_INPUT -> /INPUT_BRAKE_SWITCH_+12V_A
- J1 pad 29: /12V_GND -> /+12V_GND_A
- J1 pad 3: /ABS_HCU_VOLTAGE -> /OUTPUT_ABS_HCU_+12V_A
- J1 pad 30: /INST_CLUSTER_ABS -> /OUTPUT_INST_CLUST_ABS_+5V_B
- J1 pad 31: /INST_CLUSTER_CHARG_RED -> /OUTPUT_INST_CLUST_CHG_RED_+5V_B
- J1 pad 32: /12V_GND -> /INST_CLUSTER_GND_B
- J1 pad 33: /INST_CLUSTER_CHARGING -> /OUTPUT_INST_CLUST_CHG_+5V_B
- J1 pad 34: /INST_CLUSTER_SYS_ARMED -> /OUTPUT_INST_CLUST_ARMED_+5V_B
- J1 pad 4: /FUSE1_ABS4KEY_12VPOS -> /INPUT_ABS_HCU_POWER_+12V_A
- J1 pad 7: /POWER_PACK_GND -> /TRBATT_GND_C
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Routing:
- added copper zone on B.Cu, net /DIAG_GND
- added copper zone on F.Cu, net /DIAG_GND
- added copper zone on In1.Cu, net /DIAG_GND
- added copper zone on In2.Cu, net /DIAG_GND
- added copper zone on In3.Cu, net /DIAG_GND
- added copper zone on In4.Cu, net /DIAG_GND
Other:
- board size 160 x 80 mm -> 160 x 100 mm

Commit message: layout
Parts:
- C57, R10, R11, R16, R17, R18, R19, R20, R21, R23, R24, R25, R26, R27, R28, R29, R30, R31, R32, R33, R35, R38, R40, R44, R45, R49, R5, R50, R51, R52, R53, R6, R7, R8, R9, U1, U2, U3, U4, Z12, Z13, Z15, Z16, Z3, Z4: moved to B.Cu
- moved U1 308.2 mm to (140.6, 29.3), turned to 90 degrees
- moved R18 307.1 mm to (145.0, 28.0), turned to 90 degrees
- moved C57 293.1 mm to (142.5, 21.6), turned to -90 degrees
- moved R16 270.9 mm to (131.5, 14.0), turned to -90 degrees
- moved R17 256.6 mm to (83.0, 12.1), turned to -90 degrees
- moved R53 251.1 mm to (125.0, 25.5), turned to -90 degrees
- moved R11 250.6 mm to (120.5, 35.0), turned to 180 degrees
- moved R10 191.4 mm to (132.0, 22.0), turned to 180 degrees
- moved R27 191.3 mm to (132.0, 25.5)
- moved R34 183.0 mm to (125.5, 54.0), turned to 180 degrees
- moved R26 176.7 mm to (110.0, 13.5), turned to -90 degrees
- moved R9 176.2 mm to (137.4, 22.0), turned to 180 degrees
- moved R28 174.8 mm to (107.0, 67.5), turned to 180 degrees
- moved R30 174.5 mm to (116.0, 13.4), turned to -90 degrees
- moved R33 173.8 mm to (121.0, 17.5), turned to 180 degrees
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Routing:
- added copper zone on In2.Cu, net /Control/Isolated Canbus Module3/CAN_5V
- removed copper zone on In2.Cu, net /DIAG_GND
- removed copper zone on In3.Cu, net /DIAG_GND

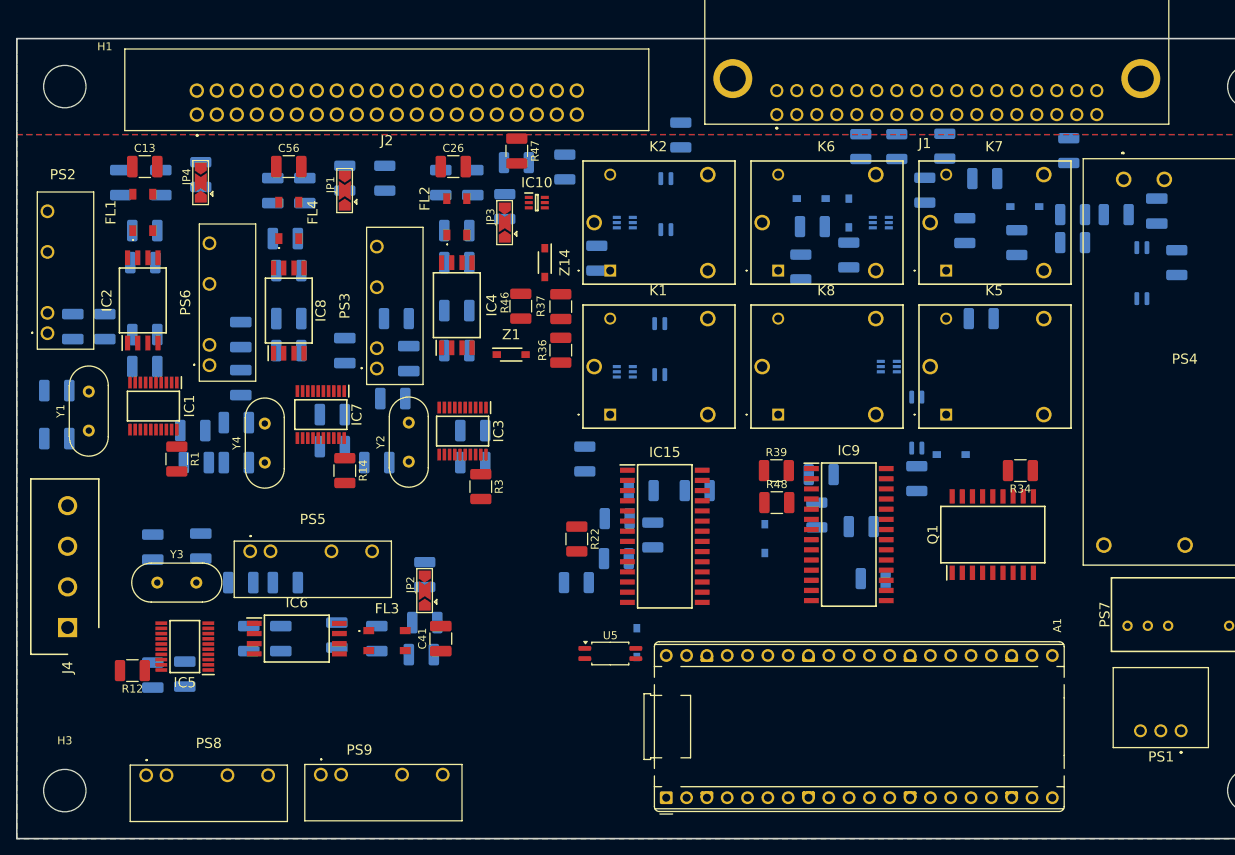
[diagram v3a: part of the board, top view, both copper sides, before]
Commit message: Update MBB Layout
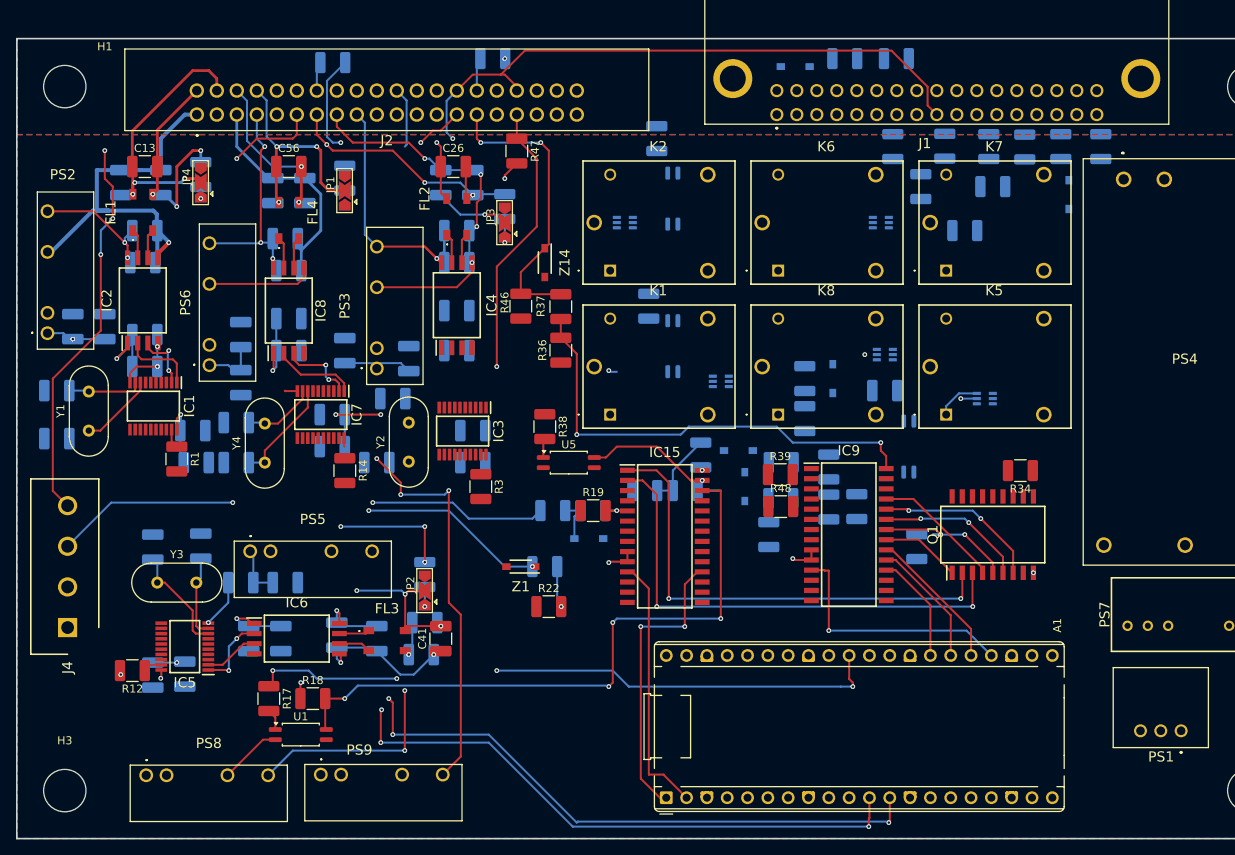
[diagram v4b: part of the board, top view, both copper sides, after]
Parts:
- IC10: moved to B.Cu
- R17, R18, R19, R38, U1: moved to F.Cu
- moved R18 121.0 mm to (37.0, 82.5), turned to 0 degrees
- moved U1 119.9 mm to (35.5, 87.0), turned to 0 degrees
- moved R17 87.3 mm to (31.5, 82.5)
- moved R9 47.8 mm to (101.5, 53.5), turned to -90 degrees
- moved R10 47.6 mm to (101.5, 58.5), turned to -90 degrees
- moved IC12 45.1 mm to (121.0, 45.0)
- moved C57 40.7 mm to (108.5, 44.0), turned to 0 degrees
- moved R23 36.1 mm to (66.0, 66.0)
- moved IC10 32.1 mm to (88.0, 42.9), turned to 180 degrees
- moved Z15 26.6 mm to (90.2, 51.5)
- moved Z1 26.5 mm to (63.0, 66.0), turned to 180 degrees
- moved R29 24.6 mm to (103.5, 2.50), turned to 0 degrees
- moved U5 24.4 mm to (69.0, 53.0)
- moved Z13 22.7 mm to (102.0, 42.5), turned to 90 degrees
- moved R11 22.1 mm to (126.0, 13.6), turned to -90 degrees
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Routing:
- net /+5V_A: track 0.00 -> 208.3 mm, vias 0 -> 5
- net /OUTPUT_MTR_CTRL_THROTTLE1_+5V_C: track 0.00 -> 170.1 mm, vias 0 -> 4
- net /UART_RX: track 0.00 -> 154.6 mm, vias 0 -> 3
- net /UART_TX: track 0.00 -> 153.4 mm, vias 0 -> 3
- net /INPUT_AMBIENT_TEMP_A: track 0.00 -> 122.0 mm, vias 0 -> 3
- net /IO_CAN2_LOW_G: track 0.00 -> 116.1 mm, vias 0 -> 6
- net /IO_CAN2_HIGH_G: track 0.00 -> 113.8 mm, vias 0 -> 4
- net /OUTPUT_HVIL_SOURCE_+5V_A: track 0.00 -> 105.4 mm, vias 0 -> 3
- net /INPUT_HVIL_RETURN_+5V_A: track 0.00 -> 94.4 mm, vias 0 -> 2
- net /IO_CAN1_HIGH_F: track 0.00 -> 84.1 mm, vias 0 -> 3
- net Net-(Z1-K): track 0.00 -> 83.0 mm, vias 0 -> 3
- net /Control/I_HVIL_STATUS_A: track 0.00 -> 82.3 mm, vias 0 -> 4
- net /IO_CAN1_LOW_F: track 0.00 -> 77.6 mm, vias 0 -> 4
- net /CAN1_GND_F: track 0.00 -> 76.4 mm, vias 0 -> 2
- net /INPUT_ABS_INDICATOR_+12V_A: track 0.00 -> 75.6 mm, vias 0 -> 1
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- added copper zone on In3.Cu, net /+12V_A
- added copper zone on In2.Cu, net /+3.3V_A
